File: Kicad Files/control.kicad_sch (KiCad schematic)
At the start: 74 parts

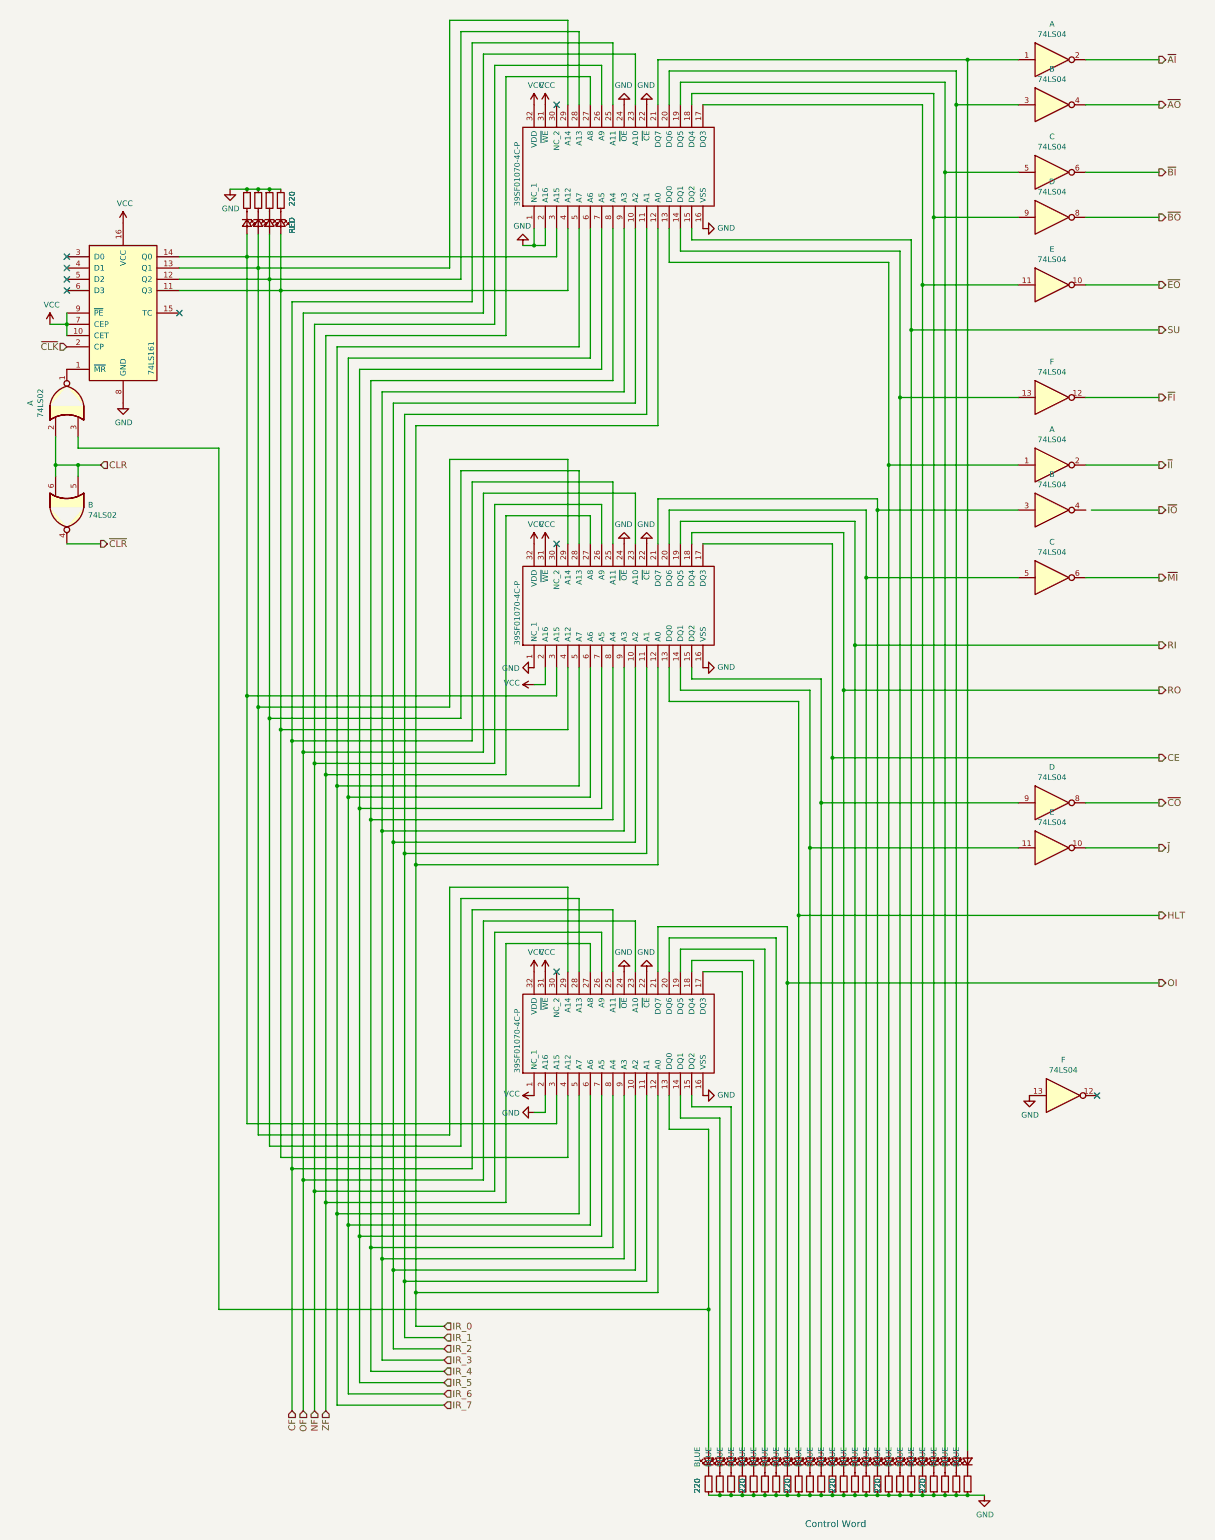
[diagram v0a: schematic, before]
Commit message: started tidy up in control
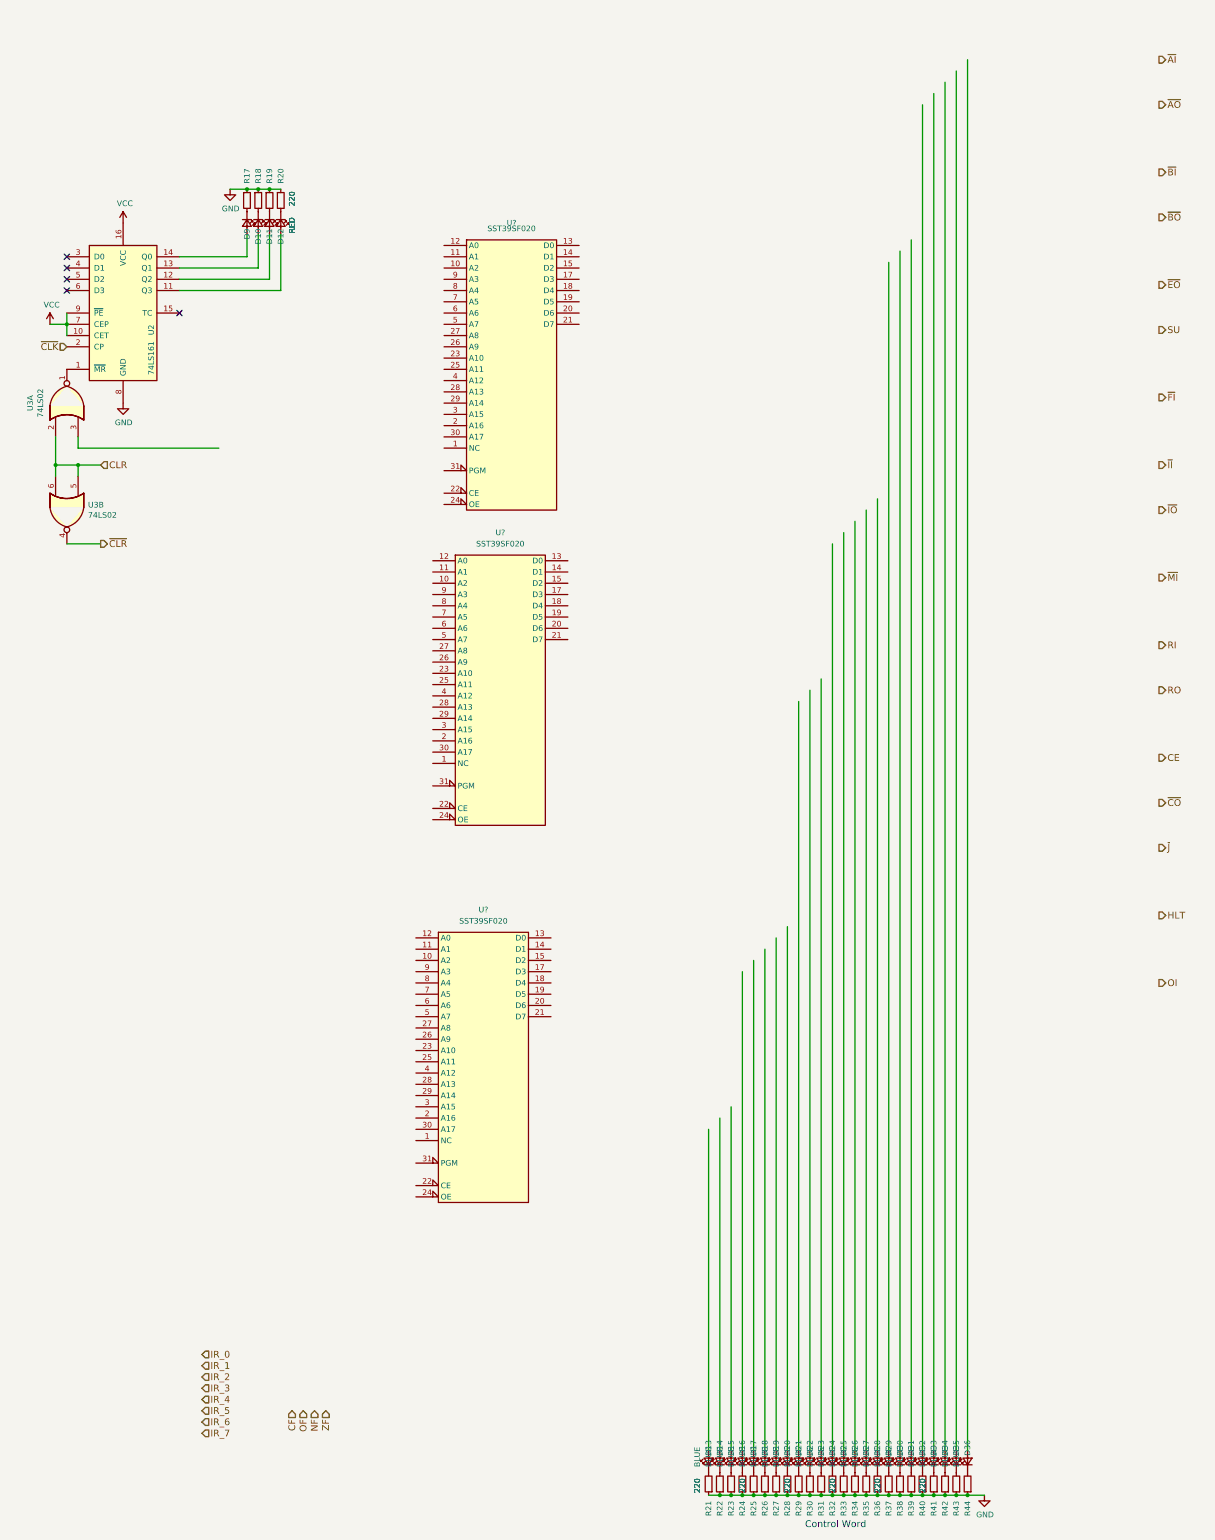
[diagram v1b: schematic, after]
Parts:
- removed ? (x3): 39SF01070-4C-P, DIP1524W56P254L4204H483Q32N, symbol 8bit-computer-rescue:39SF01070-4C-P-39SF01070-4C-P
- removed ? (x12): 74LS04, symbol 74xx:74LS04
- added U? (x3): SST39SF020, symbol Memory_Flash:SST39SF020
- gave numbers to parts that had none: 58
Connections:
- net CE: no longer D24.2 (A)
- net GND: now also U?.16 (GND), U?.16 (GND), U?.16 (GND)
- net HLT: no longer D21.2 (A)
- net OI: no longer D20.2 (A)
- net RI: no longer D26.2 (A)
- net RO: no longer D25.2 (A)
- net SU: no longer D31.2 (A)
- net VCC: now also U?.32 (VCC), U?.32 (VCC), U?.32 (VCC)
- net at U3.3: no longer D13.2 (A)
- no-connect marks 9 -> 5

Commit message: work on cl
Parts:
- removed U? (x2): SST39SF020, symbol Memory_Flash:SST39SF020
- added U? (x2): SST39SF020, symbol Memory_Flash:SST39SF020
- D66: renamed from D9; value RED -> LED_Small
- D67: renamed from D10; value RED -> LED_Small
- D68: renamed from D11; value RED -> LED_Small
- D69: renamed from D12; value RED -> LED_Small
- D70: renamed from D13; value BLUE -> LED_Small
- D71: renamed from D14; value BLUE -> LED_Small
- D72: renamed from D15; value BLUE -> LED_Small
- D73: renamed from D16; value BLUE -> LED_Small
- D74: renamed from D17; value BLUE -> LED_Small
- D75: renamed from D18; value BLUE -> LED_Small
- D76: renamed from D19; value BLUE -> LED_Small
- D77: renamed from D20; value BLUE -> LED_Small
- D78: renamed from D21; value BLUE -> LED_Small
- D79: renamed from D22; value BLUE -> LED_Small
- D80: renamed from D23; value BLUE -> LED_Small
- D81: renamed from D24; value BLUE -> LED_Small
- D82: renamed from D25; value BLUE -> LED_Small
- D83: renamed from D26; value BLUE -> LED_Small
- D84: renamed from D27; value BLUE -> LED_Small
- D85: renamed from D28; value BLUE -> LED_Small
- D86: renamed from D29; value BLUE -> LED_Small
- D87: renamed from D30; value BLUE -> LED_Small
- D88: renamed from D31; value BLUE -> LED_Small
- D89: renamed from D32; value BLUE -> LED_Small
- D90: renamed from D33; value BLUE -> LED_Small
- D91: renamed from D34; value BLUE -> LED_Small
- D92: renamed from D35; value BLUE -> LED_Small
- D93: renamed from D36; value BLUE -> LED_Small
- R101: renamed from R17; value 220 -> R_Small
- R102: renamed from R18; value 220 -> R_Small
- R103: renamed from R19; value 220 -> R_Small
- R104: renamed from R20; value 220 -> R_Small
- R105: renamed from R21; value 220 -> R_Small
- R106: renamed from R22; value 220 -> R_Small
- R107: renamed from R23; value 220 -> R_Small
- R108: renamed from R24; value 220 -> R_Small
- R109: renamed from R25; value 220 -> R_Small
- R110: renamed from R26; value 220 -> R_Small
- R111: renamed from R27; value 220 -> R_Small
- R112: renamed from R28; value 220 -> R_Small
- R113: renamed from R29; value 220 -> R_Small
- R114: renamed from R30; value 220 -> R_Small
- R115: renamed from R31; value 220 -> R_Small
- R116: renamed from R32; value 220 -> R_Small
- R117: renamed from R33; value 220 -> R_Small
- R118: renamed from R34; value 220 -> R_Small
- R119: renamed from R35; value 220 -> R_Small
- R120: renamed from R36; value 220 -> R_Small
- R121: renamed from R37; value 220 -> R_Small
- R122: renamed from R38; value 220 -> R_Small
- R123: renamed from R39; value 220 -> R_Small
- R124: renamed from R40; value 220 -> R_Small
- R125: renamed from R41; value 220 -> R_Small
- R126: renamed from R42; value 220 -> R_Small
- R127: renamed from R43; value 220 -> R_Small
- R128: renamed from R44; value 220 -> R_Small
- gave numbers to parts that had none: 1
- renumbered U3 to U45, U2 to U46
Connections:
- net CE: now also D74.2 (A), U?.17 (D3)
- net CF: now also U47.25 (A11), U?.25 (A11), U?.25 (A11)
- net GND: now also U47.2 (A16), U47.22 (CE), U47.24 (OE), U47.30 (A17), U?.16 (GND), U?.16 (GND), U?.2 (A16), U?.2 (A16), U?.22 (CE), U?.22 (CE), U?.24 (OE), U?.24 (OE), U?.30 (A17), U?.30 (A17)
- net HLT: now also D70.2 (A), U?.21 (D7)
- net IR_0: now also U47.12 (A0), U?.12 (A0), U?.12 (A0)
- net IR_1: now also U47.11 (A1), U?.11 (A1), U?.11 (A1)
- net IR_2: now also U47.10 (A2), U?.10 (A2), U?.10 (A2)
- net IR_3: now also U47.9 (A3), U?.9 (A3), U?.9 (A3)
- net IR_4: now also U47.8 (A4), U?.8 (A4), U?.8 (A4)
- net IR_5: now also U47.7 (A5), U?.7 (A5), U?.7 (A5)
- net IR_6: now also U47.6 (A6), U?.6 (A6), U?.6 (A6)
- net IR_7: now also U47.5 (A7), U?.5 (A7), U?.5 (A7)
- net NF: now also U47.26 (A9), U?.26 (A9), U?.26 (A9)
- net OF: now also U47.23 (A10), U?.23 (A10), U?.23 (A10)
- net OI: now also D71.2 (A), U?.20 (D6)
- net RI: now also D76.2 (A), U?.14 (D1)
- net RO: now also D75.2 (A), U?.15 (D2)
- net SU: now also D79.2 (A), U?.20 (D6)
- net VCC: now also U47.31 (PGM), U?.31 (PGM), U?.31 (PGM), U?.32 (VCC), U?.32 (VCC)
- net ZF: now also U47.27 (A8), U?.27 (A8), U?.27 (A8)
- net ~{AI}: now also D93.2 (A), U47.13 (D0)
- net ~{AO}: now also D92.2 (A), U47.14 (D1)
- net ~{BI}: now also D91.2 (A), U47.15 (D2)
- net ~{BO}: now also D90.2 (A), U47.17 (D3)
- net ~{CO}: now also D73.2 (A), U?.18 (D4)
- net ~{EO}: now also D80.2 (A), U?.19 (D5)
- net ~{FI}: now also D78.2 (A), U?.21 (D7)
- net ~{II}: now also D89.2 (A), U47.18 (D4)
- net ~{IO}: now also D88.2 (A), U47.19 (D5)
- net ~{J}: now also D72.2 (A), U?.19 (D5)
- net ~{MI}: now also D77.2 (A), U?.13 (D0)
- net at D81.2 (A): now also U?.18 (D4)
- net at D82.2 (A): now also U?.17 (D3)
- net at D83.2 (A): now also U?.15 (D2)
- net at D84.2 (A): now also U?.14 (D1)
- net at D85.2 (A): now also U?.13 (D0)
- net at D86.2 (A): now also U47.21 (D7)
- net at D87.2 (A): now also U47.20 (D6)
- net at D69.2 (A), U46.11 (Q3): now also U47.4 (A12), U?.4 (A12), U?.4 (A12)
- net at D68.2 (A), U46.12 (Q2): now also U47.28 (A13), U?.28 (A13), U?.28 (A13)
- net at D67.2 (A), U46.13 (Q1): now also U47.29 (A14), U?.29 (A14), U?.29 (A14)
- net at D66.2 (A), U46.14 (Q0): now also U47.3 (A15), U?.3 (A15), U?.3 (A15)
- no-connect marks 5 -> 8
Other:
- moved on the sheet: D66, D67, D68, D69, D70, D71, D72, D73, D74, D75, D76, D77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

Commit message: work on cl
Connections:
- net GND: no longer U?.2 (A16), U?.30 (A17)
- net VCC: now also U?.30 (A17)
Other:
- moved on the sheet: D66, D67, D68, D69, D70, D71, D72, D73, D74, D75, D76, D77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

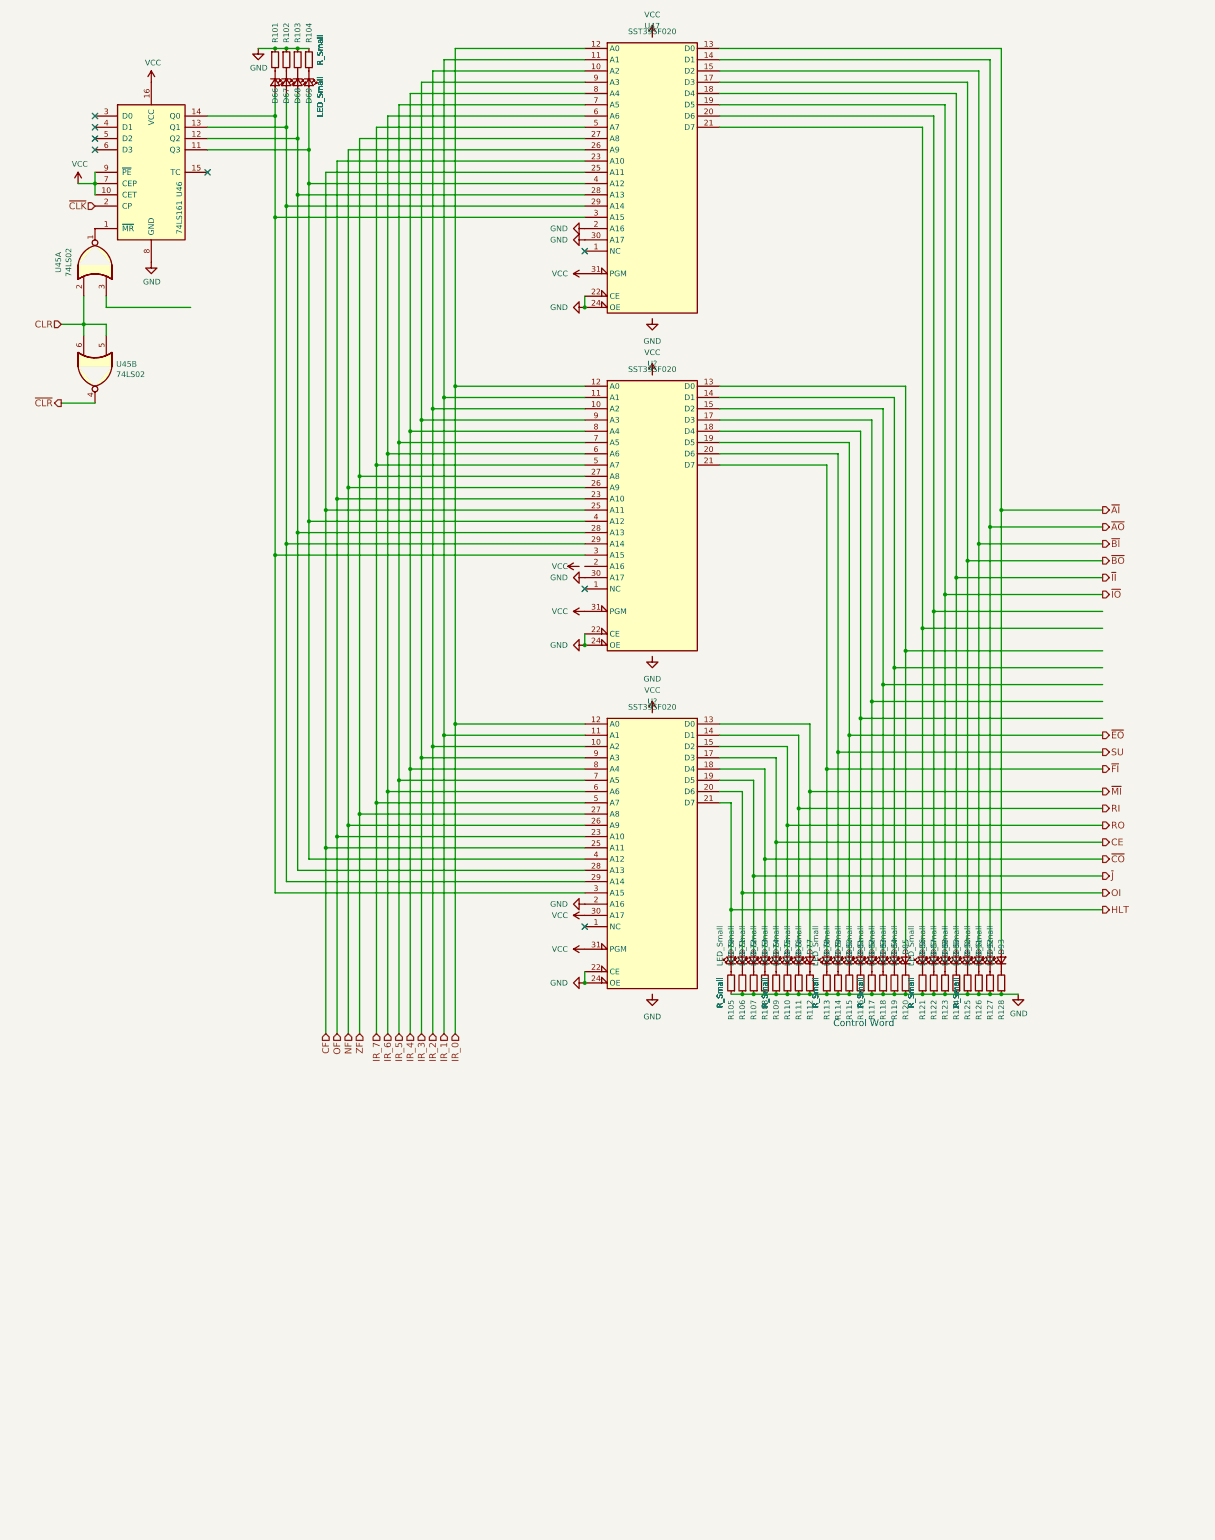
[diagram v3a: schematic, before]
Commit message: fixed ecc problems
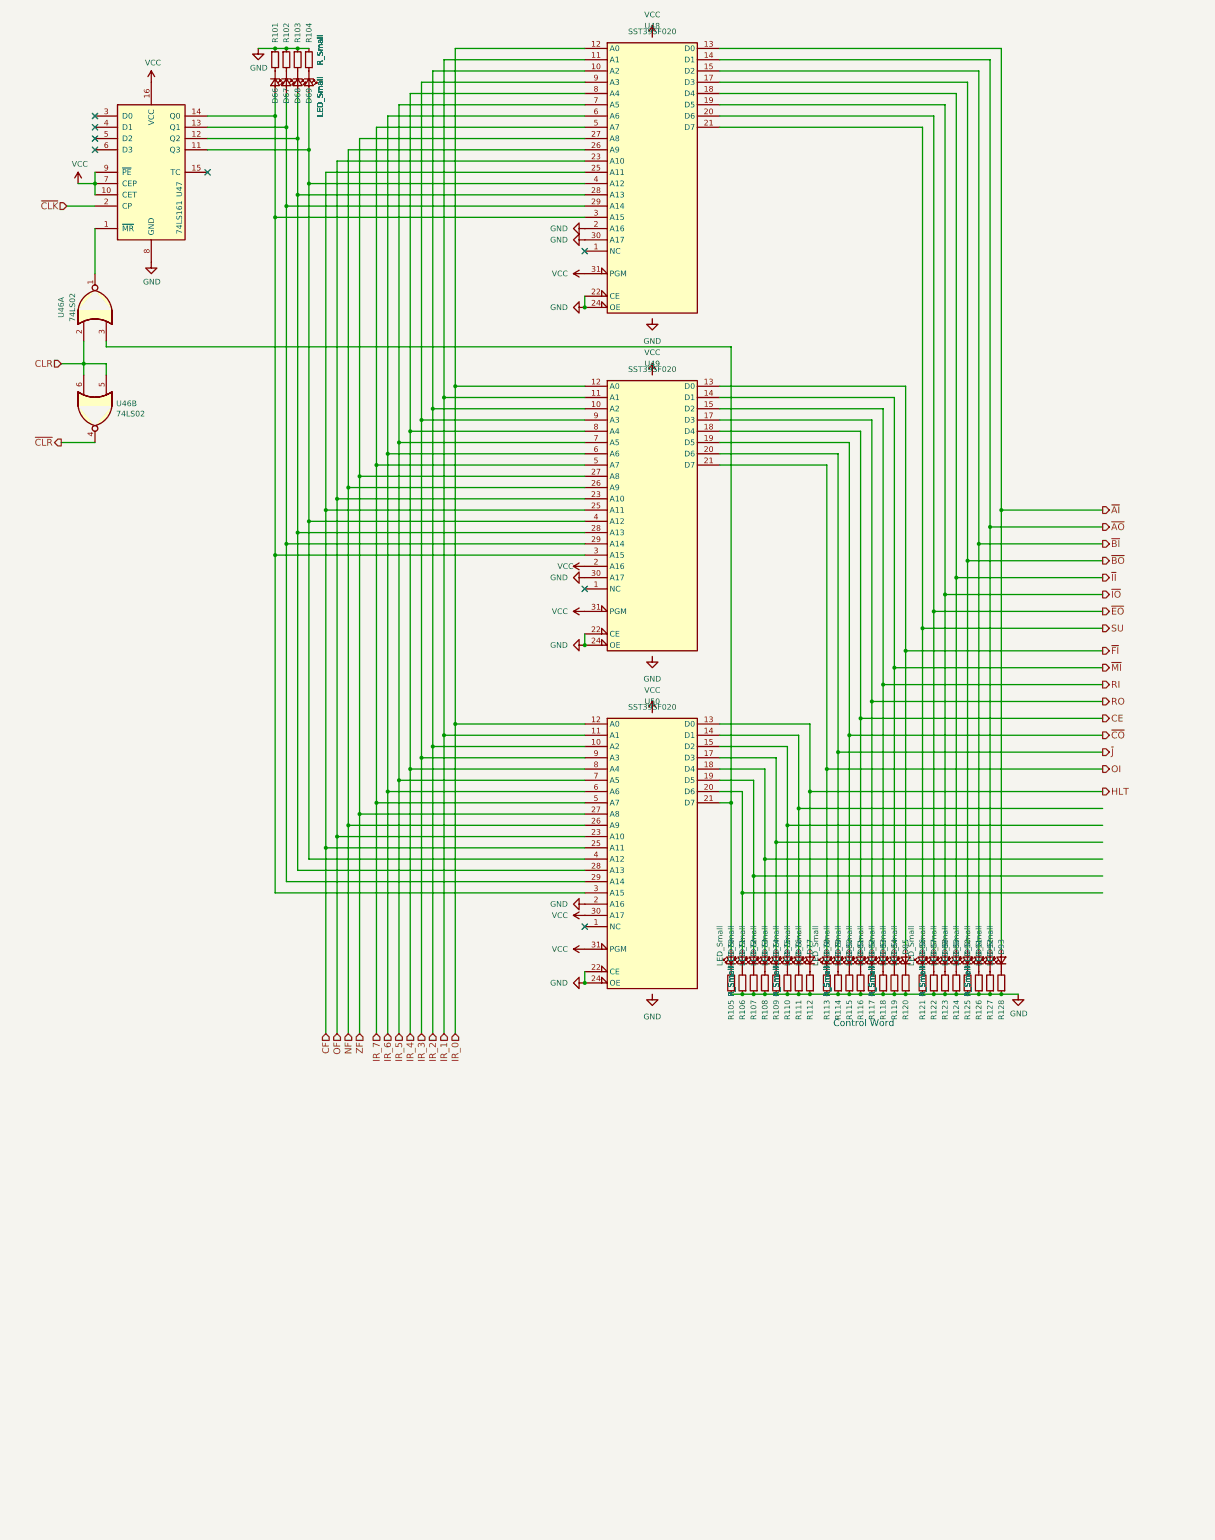
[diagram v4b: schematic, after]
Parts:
- gave numbers to parts that had none: 2
- renumbered U45 to U46, U46 to U47, U47 to U48
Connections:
- net CE: now also D81.2 (A), U49.18 (D4); no longer D74.2 (A), U50.17 (D3)
- net HLT: now also D77.2 (A), U50.13 (D0); no longer D70.2 (A), U50.21 (D7)
- net OI: now also D78.2 (A), U49.21 (D7); no longer D71.2 (A), U50.20 (D6)
- net RI: now also D83.2 (A), U49.15 (D2); no longer D76.2 (A), U50.14 (D1)
- net RO: now also D82.2 (A), U49.17 (D3); no longer D75.2 (A), U50.15 (D2)
- net SU: now also D86.2 (A), U48.21 (D7); no longer D79.2 (A), U49.20 (D6)
- net VCC: now also U49.2 (A16)
- net ~{CO}: now also D80.2 (A), U49.19 (D5); no longer D73.2 (A), U50.18 (D4)
- net ~{EO}: now also D87.2 (A), U48.20 (D6); no longer D80.2 (A), U49.19 (D5)
- net ~{FI}: now also D85.2 (A), U49.13 (D0); no longer D78.2 (A), U49.21 (D7)
- net ~{J}: now also D79.2 (A), U49.20 (D6); no longer D72.2 (A), U50.19 (D5)
- net ~{MI}: now also D84.2 (A), U49.14 (D1); no longer D77.2 (A), U50.13 (D0)
- net at U46.3: now also D70.2 (A), U50.21 (D7)
- new net: D71.2 (A), U50.20 (D6)
- new net: D72.2 (A), U50.19 (D5)
- new net: D73.2 (A), U50.18 (D4)
- new net: D74.2 (A), U50.17 (D3)
- new net: D75.2 (A), U50.15 (D2)
- new net: D76.2 (A), U50.14 (D1)
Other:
- moved on the sheet: U46A, U46B
